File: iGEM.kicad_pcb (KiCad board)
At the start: 4 copper layers, 85 x 60 mm, 50 parts, among them IC1 TMCS1107A1BQDRQ1, IC2 TMCS1107A1BQDRQ1, IC3 MCP4642-502E_UN, J1 Conn_01x02, J2 Conn_01x02, J3 Conn_01x02, J4 Conn_01x03, M1 Fan, Q1 TIP122, Q2 TIP122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

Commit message: mounting holes no longer connected to signal ground because the chassis will be connected to true earth
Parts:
- R10, R9: value 5K -> 4.7K
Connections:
- H1 pad 1: GND -> unconnected-(H1-Pad1)
- H2 pad 1: GND -> unconnected-(H2-Pad1)
- H3 pad 1: GND -> unconnected-(H3-Pad1)
- H4 pad 1: GND -> unconnected-(H4-Pad1)
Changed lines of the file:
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@@
   (net 32 "Net-(D4-Pad1)")
   (net 33 "Net-(D4-Pad2)")
+  (net 34 "unconnected-(H1-Pad1)")
+  (net 35 "unconnected-(H2-Pad1)")
+  (net 36 "unconnected-(H3-Pad1)")
+  (net 37 "unconnected-(H4-Pad1)")
   (footprint "Package_TO_SOT_SMD:SOT-23-6" (layer "F.Cu")
     (at 136.5 70.5)
@@
     (fp_circle (center 0 0) (end 4.85 0) (layer "F.CrtYd") (width 0.05) (fill none))
     (pad "1" thru_hole circle (at 0 0) (size 9.2 9.2) (drill 5.3) (layers *.Cu *.Mask)
-      (net 2 "GND") (pinfunction "1") (pintype "input"))
+      (net 36 "unconnected-(H3-Pad1)") (pinfunction "1") (pintype "input+no_connect"))
   )
   (footprint "Package_TO_SOT_SMD:SOT-23-6" (layer "F.Cu")
@@
     (descr "Capacitor SMD 0805 (2012 Metric), square (rectangular) end terminal, IPC_7351 nominal with elongated pad for handsoldering. (Body size source: IPC-SM-782 page 76, https://www.pcb-3d.com/wordpress/wp-content/uploads/ipc-sm-782a_amendment_1_and_2.pdf, https://docs.google.com/spreadsheets/d/1BsfQQcO9C6DZCsRaXUlFlo91Tg2WpOkGARC1WS5S8t0/edit?usp=sharing), generated with kicad-footprint-generator")
     (tags "capacitor handsolder")
+    (property "DigiKey" "399-C0805C104K8RAC7800CT-ND")
     (property "Sheetfile" "iGEM.kicad_sch")
     (property "Sheetname" "")
@@
     (descr "Capacitor SMD 0805 (2012 Metric), square (rectangular) end terminal, IPC_7351 nominal with elongated pad for handsoldering. (Body size source: IPC-SM-782 page 76, https://www.pcb-3d.com/wordpress/wp-content/uploads/ipc-sm-782a_amendment_1_and_2.pdf, https://docs.google.com/spreadsheets/d/1BsfQQcO9C6DZCsRaXUlFlo91Tg2WpOkGARC1WS5S8t0/edit?usp=sharing), generated with kicad-footprint-generator")
     (tags "capacitor handsolder")
+    (property "DigiKey" "399-C0805C104K8RAC7800CT-ND")
     (property "Sheetfile" "iGEM.kicad_sch")
     (property "Sheetname" "")
@@
     (descr "Capacitor SMD 0805 (2012 Metric), square (rectangular) end terminal, IPC_7351 nominal with elongated pad for handsoldering. (Body size source: IPC-SM-782 page 76, https://www.pcb-3d.com/wordpress/wp-content/uploads/ipc-sm-782a_amendment_1_and_2.pdf, https://docs.google.com/spreadsheets/d/1BsfQQcO9C6DZCsRaXUlFlo91Tg2WpOkGARC1WS5S8t0/edit?usp=sharing), generated with kicad-footprint-generator")
     (tags "capacitor handsolder")
+    (property "DigiKey" "399-C0805C104K8RAC7800CT-ND")
     (property "Sheetfile" "iGEM.kicad_sch")
     (property "Sheetname" "")
@@
     (descr "JST XH series connector, B2B-XH-AM, with boss (http://www.jst-mfg.com/product/pdf/eng/eXH.pdf), generated with kicad-footprint-generator")
     (tags "connector JST XH vertical boss")
+    (property "DigiKey" "455-2879-ND")
     (property "Sheetfile" "iGEM.kicad_sch")
     (property "Sheetname" "")
@@
     (descr "Resistor SMD 0805 (2012 Metric), square (rectangular) end terminal, IPC_7351 nominal with elongated pad for handsoldering. (Body size source: IPC-SM-782 page 72, https://www.pcb-3d.com/wordpress/wp-content/uploads/ipc-sm-782a_amendment_1_and_2.pdf), generated with kicad-footprint-generator")
     (tags "resistor handsolder")
+    (property "DigiKey" "RMCF0805FT4K70CT-ND")
     (property "Sheetfile" "iGEM.kicad_sch")
     (property "Sheetname" "")
@@
       (effects (font (size 1 1) (thickness 0.15)))
     )
-    (fp_text value "5K" (at 0 1.65) (layer "F.Fab")
+    (fp_text value "4.7K" (at 0 1.65) (layer "F.Fab")
       (effects (font (size 1 1) (thickness 0.15)))
     )
@@
     (fp_circle (center 0 0) (end 4.85 0) (layer "F.CrtYd") (width 0.05) (fill none))
     (pad "1" thru_hole circle (at 0 0) (size 9.2 9.2) (drill 5.3) (layers *.Cu *.Mask)
-      (net 2 "GND") (pinfunction "1") (pintype "input"))
+      (net 37 "unconnected-(H4-Pad1)") (pinfunction "1") (pintype "input+no_connect"))
   )
   (footprint "TerminalBlock:TerminalBlock_bornier-2_P5.08mm" (layer "F.Cu")
@@
     (descr "Resistor SMD 0805 (2012 Metric), square (rectangular) end terminal, IPC_7351 nominal with elongated pad for handsoldering. (Body size source: IPC-SM-782 page 72, https://www.pcb-3d.com/wordpress/wp-content/uploads/ipc-sm-782a_amendment_1_and_2.pdf), generated with kicad-footprint-generator")
     (tags "resistor handsolder")
+    (property "DigiKey" "RMCF0805FT4K70CT-ND")
     (property "Sheetfile" "iGEM.kicad_sch")
     (property "Sheetname" "")
@@
       (effects (font (size 1 1) (thickness 0.15)))
     )
-    (fp_text value "5K" (at 0 1.65) (layer "F.Fab")
+    (fp_text value "4.7K" (at 0 1.65) (layer "F.Fab")
       (effects (font (size 1 1) (thickness 0.15)))
     )
@@
     (fp_circle (center 0 0) (end 4.85 0) (layer "F.CrtYd") (width 0.05) (fill none))
     (pad "1" thru_hole circle (at 0 0) (size 9.2 9.2) (drill 5.3) (layers *.Cu *.Mask)
-      (net 2 "GND") (pinfunction "1") (pintype "input"))
+      (net 35 "unconnected-(H2-Pad1)") (pinfunction "1") (pintype "input+no_connect"))
   )
   (footprint "Package_TO_SOT_THT:TO-220-3_Vertical" (layer "F.Cu")
@@
     (descr "Capacitor SMD 0805 (2012 Metric), square (rectangular) end terminal, IPC_7351 nominal with elongated pad for handsoldering. (Body size source: IPC-SM-782 page 76, https://www.pcb-3d.com/wordpress/wp-content/uploads/ipc-sm-782a_amendment_1_and_2.pdf, https://docs.google.com/spreadsheets/d/1BsfQQcO9C6DZCsRaXUlFlo91Tg2WpOkGARC1WS5S8t0/edit?usp=sharing), generated with kicad-footprint-generator")
     (tags "capacitor handsolder")
+    (property "DigiKey" "399-C0805C104K8RAC7800CT-ND")
     (property "Sheetfile" "iGEM.kicad_sch")
     (property "Sheetname" "")
@@
     (fp_circle (center 0 0) (end 4.85 0) (layer "F.CrtYd") (width 0.05) (fill none))
     (pad "1" thru_hole circle (at 0 0) (size 9.2 9.2) (drill 5.3) (layers *.Cu *.Mask)
-      (net 2 "GND") (pinfunction "1") (pintype "input"))
+      (net 34 "unconnected-(H1-Pad1)") (pinfunction "1") (pintype "input+no_connect"))
   )
   (footprint "Capacitor_SMD:C_0805_2012Metric_Pad1.18x1.45mm_HandSolder" (layer "F.Cu")
@@
     (descr "Capacitor SMD 0805 (2012 Metric), square (rectangular) end terminal, IPC_7351 nominal with elongated pad for handsoldering. (Body size source: IPC-SM-782 page 76, https://www.pcb-3d.com/wordpress/wp-content/uploads/ipc-sm-782a_amendment_1_and_2.pdf, https://docs.google.com/spreadsheets/d/1BsfQQcO9C6DZCsRaXUlFlo91Tg2WpOkGARC1WS5S8t0/edit?usp=sharing), generated with kicad-footprint-generator")
     (tags "capacitor handsolder")
+    (property "DigiKey" "399-C0805C104K8RAC7800CT-ND")
     (property "Sheetfile" "iGEM.kicad_sch")
     (property "Sheetname" "")
@@
     (descr "Capacitor SMD 0805 (2012 Metric), square (rectangular) end terminal, IPC_7351 nominal with elongated pad for handsoldering. (Body size source: IPC-SM-782 page 76, https://www.pcb-3d.com/wordpress/wp-content/uploads/ipc-sm-782a_amendment_1_and_2.pdf, https://docs.google.com/spreadsheets/d/1BsfQQcO9C6DZCsRaXUlFlo91Tg2WpOkGARC1WS5S8t0/edit?usp=sharing), generated with kicad-footprint-generator")
     (tags "capacitor handsolder")
+    (property "DigiKey" "399-C0805C104K8RAC7800CT-ND")
     (property "Sheetfile" "iGEM.kicad_sch")
     (property "Sheetname" "")
@@
     (descr "Capacitor SMD 0805 (2012 Metric), square (rectangular) end terminal, IPC_7351 nominal with elongated pad for handsoldering. (Body size source: IPC-SM-782 page 76, https://www.pcb-3d.com/wordpress/wp-content/uploads/ipc-sm-782a_amendment_1_and_2.pdf, https://docs.google.com/spreadsheets/d/1BsfQQcO9C6DZCsRaXUlFlo91Tg2WpOkGARC1WS5S8t0/edit?usp=sharing), generated with kicad-footprint-generator")
     (tags "capacitor handsolder")
-    (property "Sheetfile" "iGEM.kicad_sch")
-    (property "Sheetname" "")
+    (property "DigiKey" "399-C0805C104K8RAC7800CT-ND")
+    (property "Sheetfile" "iGEM.kicad_sch")
+    (property "Sheetname" "")

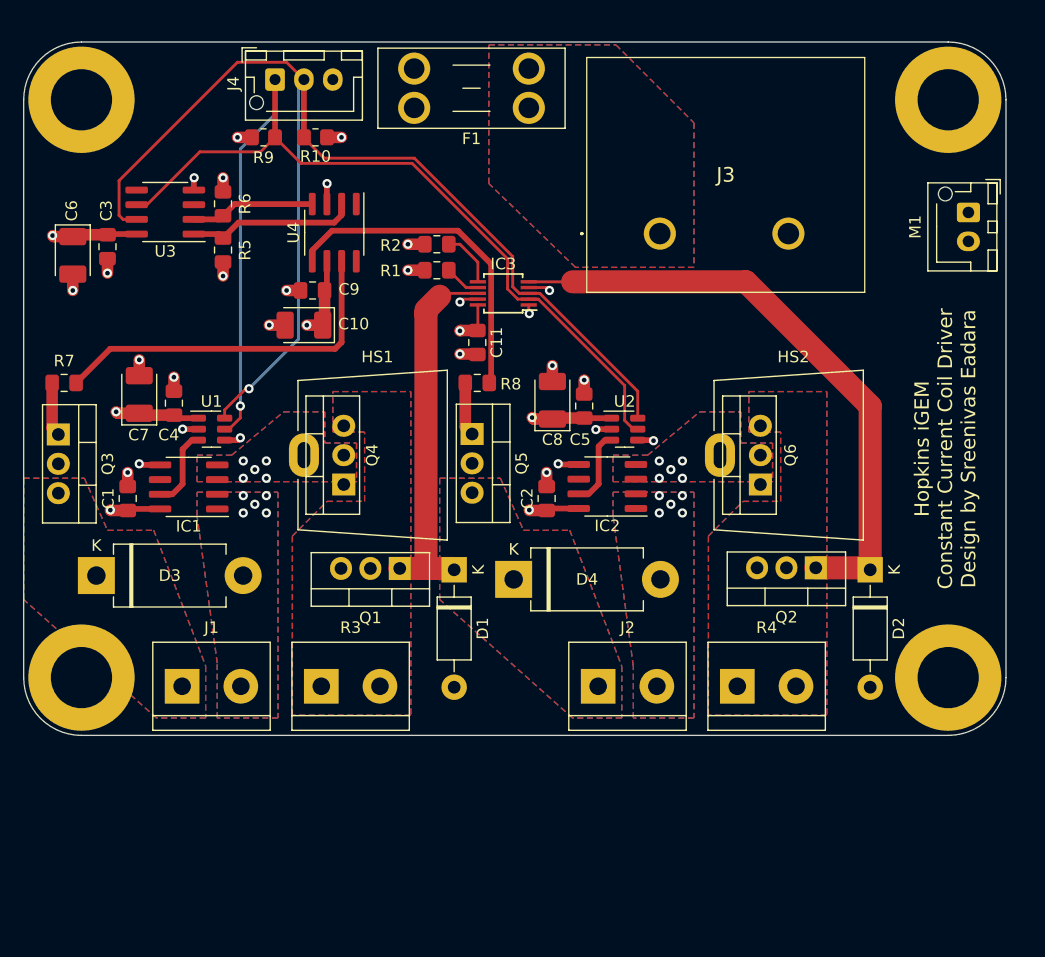
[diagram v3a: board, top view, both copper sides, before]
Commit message: updated mounting holes to M3
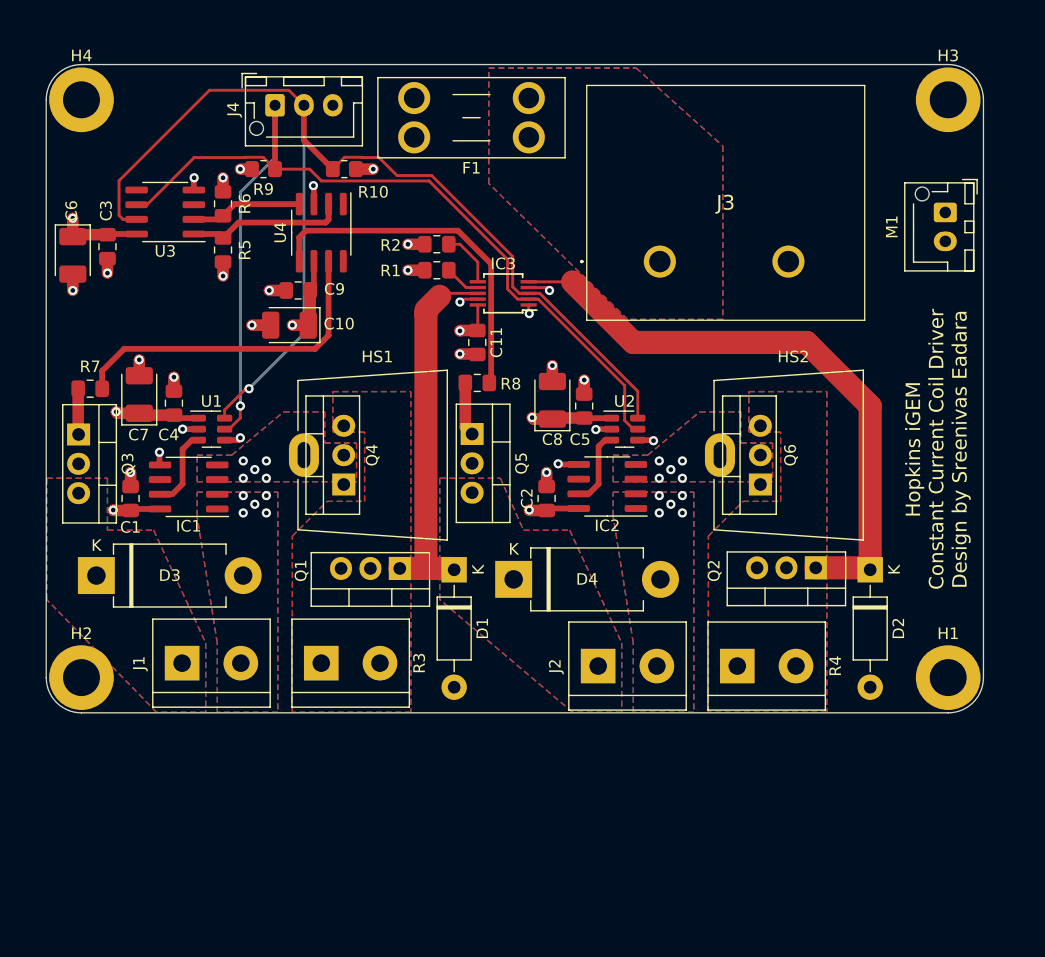
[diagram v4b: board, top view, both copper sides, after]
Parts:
- H1, H2, H3, H4: footprint MountingHole:MountingHole_5.3mm_M5_DIN965_Pad -> MountingHole:MountingHole_3.2mm_M3_DIN965_Pad
- moved R10 3.72 mm to (148.0, 48.0)
- moved R9 2.75 mm to (141.0, 48.0)
- moved F1 2.55 mm to (164.0, 45.2)
- moved J3 2.42 mm to (175.3, 56.0)
- moved R7 2.30 mm to (126.0, 67.0)
- moved J4 2.23 mm to (142.0, 42.5)
- moved J1 2.00 mm to (134.0, 90.8)
- moved M1 2.00 mm to (200.0, 51.8)
- moved R3 2.00 mm to (146.0, 90.8)
- moved Q3 1.75 mm to (125.0, 71.0)
- moved R4 1.75 mm to (182.0, 91.0)
- moved J2 1.75 mm to (170.0, 91.0)
- moved C10 1.25 mm to (143.2, 61.5)
- moved C9 1.25 mm to (144.0, 58.5)
- moved U4 1.12 mm to (146.0, 53.5)
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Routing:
- net SDA: track 104.7 -> 100.1 mm
- net SCL: track 96.8 -> 93.7 mm
- net Net-(R7-Pad1): track 31.4 -> 28.8 mm
- net Net-(R8-Pad2): track 28.7 -> 30.5 mm
- net PWM2: track 10.8 -> 9.67 mm
- net PWM1: track 14.7 -> 13.8 mm
- net FET1: track 4.68 -> 3.98 mm
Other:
- board size 85 x 60 mm -> 81.1 x 56.1 mm

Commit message: layout cleanup
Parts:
- moved R5 1.00 mm to (138.5, 55.0)
- moved R6 1.00 mm to (138.5, 51.0)
- moved R10 0.50 mm to (148.0, 47.5)
- moved R9 0.50 mm to (141.0, 47.5)
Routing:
- net SCL: track 93.7 -> 92.7 mm
- net SDA: track 100.1 -> 99.4 mm
- net GND: track 31.4 -> 31.9 mm

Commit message: increased current capacity and added useful silk
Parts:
- J4: footprint Connector_JST:JST_XH_B3B-XH-AM_1x03_P2.50mm_Vertical -> Connector_JST:JST_XH_B3B-XH-A_1x03_P2.50mm_Vertical
- M1: footprint Connector_JST:JST_XH_B2B-XH-AM_1x02_P2.50mm_Vertical -> Connector_JST:JST_XH_B2B-XH-A_1x02_P2.50mm_Vertical
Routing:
- net Net-(Q6-Pad3): vias 0 -> 15
- net Net-(Q4-Pad3): vias 0 -> 16
- net Net-(F1-Pad1): vias 0 -> 14
- net Net-(D4-Pad2): vias 5 -> 10
- net Net-(D4-Pad1): vias 0 -> 20
- net Net-(D3-Pad2): vias 5 -> 9
- net Net-(D3-Pad1): vias 0 -> 12
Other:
- board text added: "+"
- board text added: "-"
- board text added: "GND"
- board text added: "SCL"
- board text added: "SDA"
